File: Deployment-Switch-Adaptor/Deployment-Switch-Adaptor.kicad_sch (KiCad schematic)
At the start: 2 parts, among them J1 Hirose_DF11-4DP-2DSA_2x02, J2 D2F-5L3

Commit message: Deleted Lock Files
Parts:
- J2: footprint (none) -> proves-peripherals:D2F-5L3
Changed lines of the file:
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@@
 			)
 		)
-		(property "Footprint" ""
+		(property "Footprint" "proves-peripherals:D2F-5L3"
 			(at 113.03 53.34 0)
 			(effects

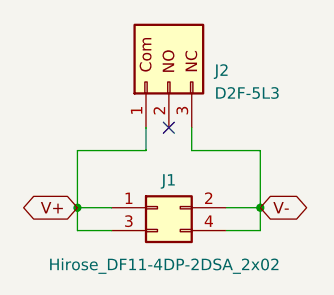
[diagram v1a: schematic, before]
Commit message: Updated with official D2F-L Footprint
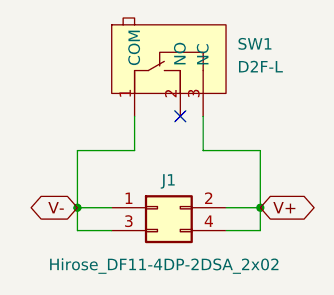
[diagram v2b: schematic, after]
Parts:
- removed J2: D2F-5L3, proves-peripherals:D2F-5L3, symbol Connector_Generic:Conn_01x03
- added SW1: D2F-L, easyeda2kicad:SW-TH_D2F-L, symbol easyeda2kicad:D2F-L
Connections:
- net V+: now also J1.2 (Pin_2), J1.4 (Pin_4), SW1.3 (NC); no longer J1.1 (Pin_1), J1.3 (Pin_3)
- net V-: now also J1.1 (Pin_1), J1.3 (Pin_3), SW1.1 (COM); no longer J1.2 (Pin_2), J1.4 (Pin_4)
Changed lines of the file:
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@@
 	)
 	(no_connect
-		(at 113.03 58.42)
+		(at 114.3 57.15)
+	)
+	(wire
+		(pts
+			(xy 116.84 57.15) (xy 116.84 60.96)
+		)
+		(stroke
+			(width 0)
+			(type default)
+		)
 	)
 	(wire
@@
 	(wire
 		(pts
-			(xy 110.49 60.96) (xy 110.49 58.42)
-		)
-		(stroke
-			(width 0)
-			(type default)
-		)
-	)
-	(wire
-		(pts
 			(xy 102.87 67.31) (xy 102.87 69.85)
 		)
@@
 	(wire
 		(pts
-			(xy 115.57 60.96) (xy 123.19 60.96)
-		)
-		(stroke
-			(width 0)
-			(type default)
-		)
-	)
-	(wire
-		(pts
 			(xy 119.38 67.31) (xy 123.19 67.31)
 		)
@@
 	(wire
 		(pts
-			(xy 102.87 60.96) (xy 110.49 60.96)
+			(xy 116.84 60.96) (xy 123.19 60.96)
 		)
 		(stroke
@@
 	(wire
 		(pts
-			(xy 115.57 58.42) (xy 115.57 60.96)
+			(xy 102.87 60.96) (xy 109.22 60.96)
+		)
+		(stroke
+			(width 0)
+			(type default)
+		)
+	)
+	(wire
+		(pts
+			(xy 109.22 57.15) (xy 109.22 60.96)
 		)
 		(stroke
@@
 		)
 	)
-	(global_label "V-"
+	(global_label "V+"
 		(shape bidirectional)
 		(at 123.19 67.31 0)
@@
 		)
 	)
-	(global_label "V+"
+	(global_label "V-"
 		(shape bidirectional)
 		(at 102.87 67.31 180)
@@
 	)
 	(symbol
-		(lib_id "Connector_Generic:Conn_01x03")
-		(at 113.03 53.34 90)
+		(lib_id "easyeda2kicad:D2F-L")
+		(at 114.3 52.07 0)
 		(unit 1)
 		(exclude_from_sim no)
@@
 		(dnp no)
 		(fields_autoplaced yes)
-		(property "Reference" "J2"
-			(at 118.11 52.0699 90)
-			(effects
-				(font
-					(size 1.27 1.27)
-				)
-				(justify right)
-			)
-		)
-		(property "Value" "D2F-5L3"
-			(at 118.11 54.6099 90)
-			(effects
-				(font
-					(size 1.27 1.27)
-				)
-				(justify right)
-			)
-		)
-		(property "Footprint" "proves-peripherals:D2F-5L3"
-			(at 113.03 53.34 0)
-			(effects
-				(font
-					(size 1.27 1.27)
-				)
-				(hide yes)
-			)
-		)
-		(property "Datasheet" "~"
-			(at 113.03 53.34 0)
-			(effects
-				(font
-					(size 1.27 1.27)
-				)
-				(hide yes)
-			)
-		)
-		(property "Description" "Generic connector, single row, 01x03, script generated (kicad-library-utils/schlib/autogen/connector/)"
-			(at 113.03 53.34 0)
-			(effects
-				(font
-					(size 1.27 1.27)
-				)
-				(hide yes)
-			)
+		(property "Reference" "SW1"
+			(at 120.65 49.1499 0)
+			(effects
+				(font
+					(size 1.27 1.27)
+				)
+				(justify left)
+			)
+		)
+		(property "Value" "D2F-L"
+			(at 120.65 51.6899 0)
+			(effects
+				(font
+					(size 1.27 1.27)
+				)
+				(justify left)
+			)
+		)
+		(property "Footprint" "easyeda2kicad:SW-TH_D2F-L"
+			(at 114.3 64.77 0)
+			(effects
+				(font
+					(size 1.27 1.27)
+				)
+				(hide yes)
+			)
+		)
+		(property "Datasheet" "https://lcsc.com/product-detail/Others_Omron-Electronics_D2F-L_Omron-Electronics-D2F-L_C231337.html"
+			(at 114.3 67.31 0)
+			(effects
+				(font
+					(size 1.27 1.27)
+				)
+				(hide yes)
+			)
+		)
+		(property "Description" ""
+			(at 114.3 52.07 0)
+			(effects
+				(font
+					(size 1.27 1.27)
+				)
+				(hide yes)
+			)
+		)
+		(property "LCSC Part" "C231337"
+			(at 114.3 69.85 0)
+			(effects
+				(font
+					(size 1.27 1.27)
+				)
+				(hide yes)
+			)
+		)
+		(pin "1"
+		)
+		(pin "3"
 		)
 		(pin "2"
-		)
-		(pin "3"
-		)
-		(pin "1"
 		)
 		(instances
 			(project ""
 				(path "/fd62f8d6-bc17-47bc-8a5d-c79216a03161"
-					(reference "J2")
+					(reference "SW1")
 					(unit 1)
 				)
